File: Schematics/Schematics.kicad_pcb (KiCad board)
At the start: 2 copper layers, 60.5 x 84 mm, 14 parts, among them U1 XIAO ESP32C3, U2 TP4056-42-ESOP8

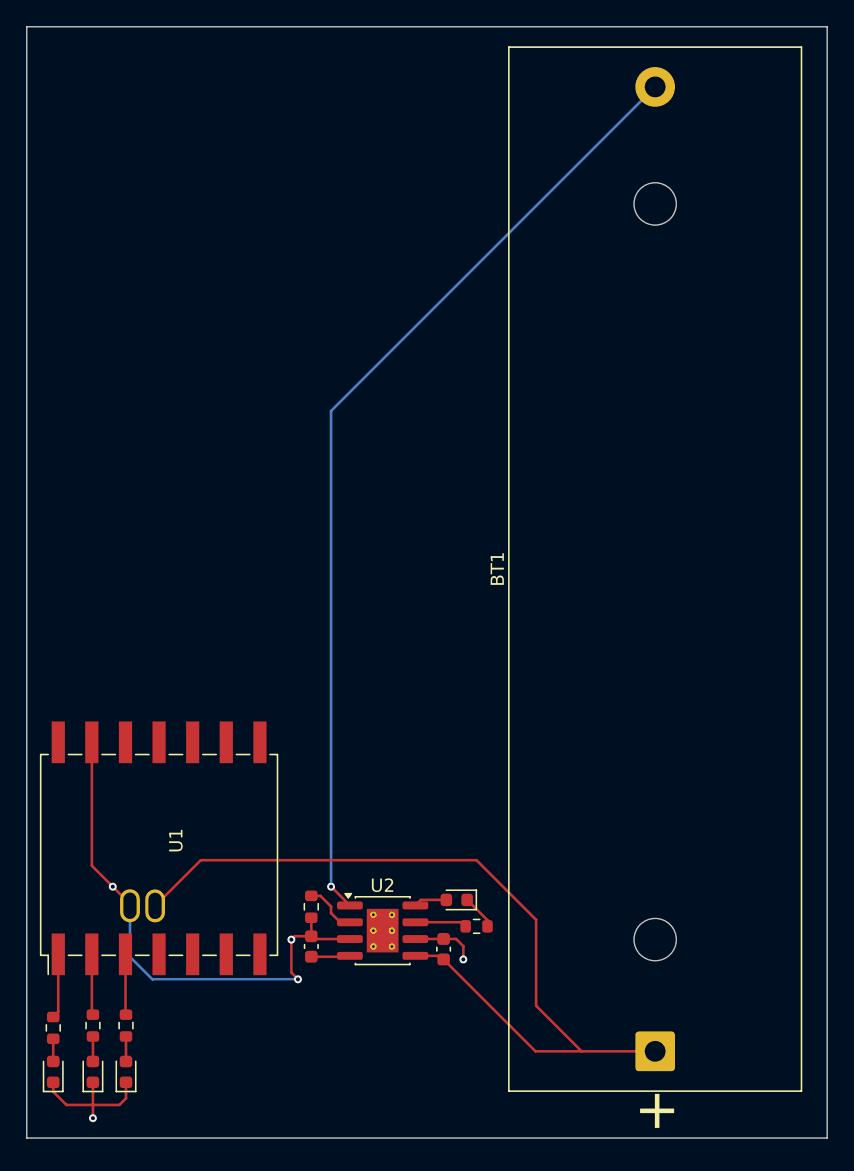
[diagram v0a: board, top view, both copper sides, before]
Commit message: redesign of the display and LEDs
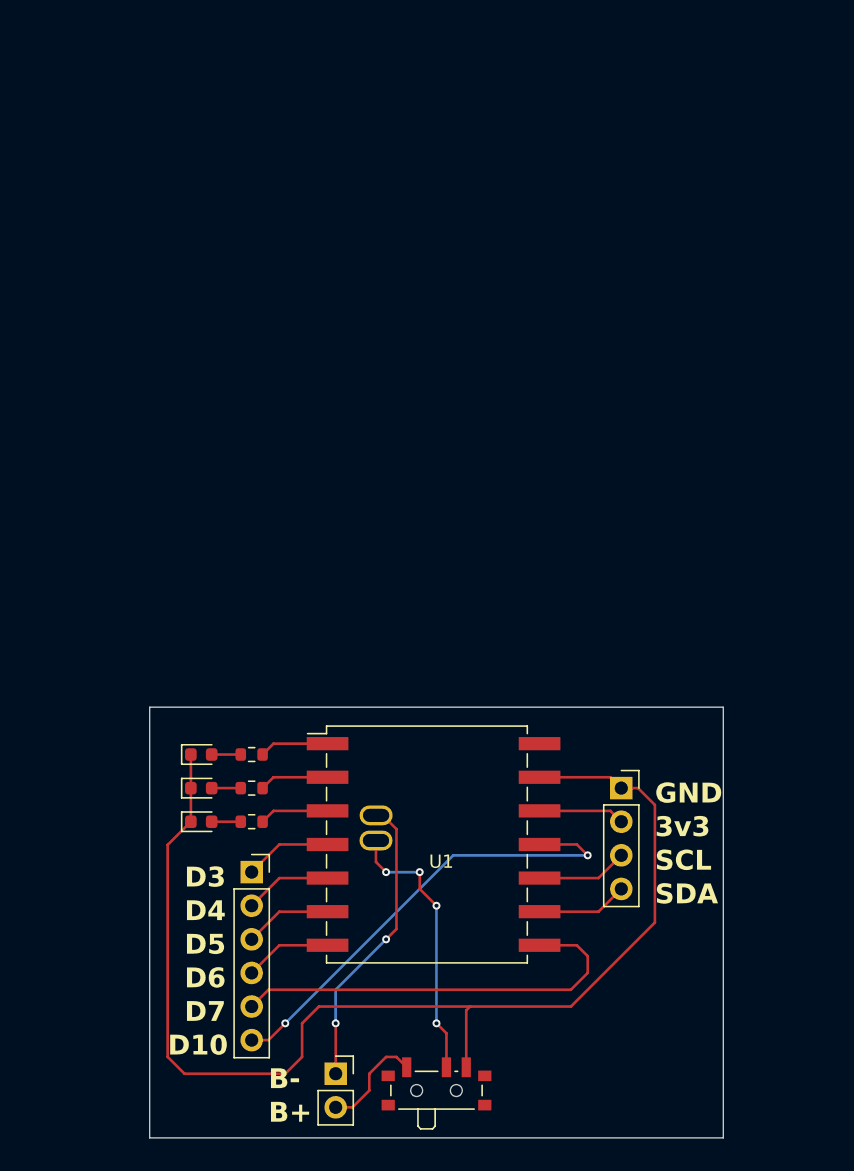
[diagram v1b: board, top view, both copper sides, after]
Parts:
- removed BT1: Battery_Cell, Battery:BatteryHolder_MPD_BH-18650-PC
- removed C1, C2: 10uF, Capacitor_SMD:C_0603_1608Metric
- removed D1: LED, LED_SMD:LED_0603_1608Metric
- removed R1: 10k, Resistor_SMD:R_0603_1608Metric
- removed R2: 1K, Resistor_SMD:R_0603_1608Metric
- removed U2: TP4056-42-ESOP8, Package_SO:SOIC-8-1EP_3.9x4.9mm_P1.27mm_EP2.41x3.3mm_ThermalVias
- added J1: Conn_01x04_Socket, Connector_PinSocket_2.54mm:PinSocket_1x04_P2.54mm_Vertical, F.Cu at (154.9, 82.5)
- added J2: Conn_01x06_Socket, Connector_PinSocket_2.54mm:PinSocket_1x06_P2.54mm_Vertical, F.Cu at (127.0, 88.9)
- added J3: Conn_01x02_Socket, Connector_PinSocket_2.54mm:PinSocket_1x02_P2.54mm_Vertical, F.Cu at (133.3, 104.1)
- added SW1: SW_SPDT, Button_Switch_SMD:SW_SPDT_PCM12, F.Cu at (141.0, 105.1)
- moved D2 26.5 mm to (123.2, 80.0), turned to 0 degrees
- moved R3 25.5 mm to (127.0, 80.0), turned to 0 degrees
- moved D3 23.0 mm to (123.2, 82.5), turned to 0 degrees
- moved R4 21.6 mm to (127.0, 82.5), turned to 0 degrees
- moved D4 19.7 mm to (123.2, 85.1), turned to 0 degrees
- moved U1 19.6 mm to (141.3, 88.6), turned to 0 degrees
- moved R5 18.1 mm to (127.0, 85.1), turned to 0 degrees
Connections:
- U1 pad 10: unconnected-(U1-D9-Pad10) -> Net-(J1-Pin_3)
- U1 pad 11: unconnected-(U1-D10-Pad11) -> Net-(J2-Pin_6)
- U1 pad 12: unconnected-(U1-VCC_3V3-Pad12) -> Net-(J1-Pin_2)
- U1 pad 4: unconnected-(U1-D3-Pad4) -> Net-(J2-Pin_1)
- U1 pad 5: unconnected-(U1-D4-Pad5) -> Net-(J2-Pin_2)
- U1 pad 6: unconnected-(U1-D5-Pad6) -> Net-(J2-Pin_3)
- U1 pad 7: unconnected-(U1-D6-Pad7) -> Net-(J2-Pin_4)
- U1 pad 8: unconnected-(U1-D7-Pad8) -> Net-(J2-Pin_5)
- U1 pad 9: unconnected-(U1-D8-Pad9) -> Net-(J1-Pin_4)
- U1 pad B-: GND -> Net-(J3-Pin_1)
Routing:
- net Net-(SW1-B): track 64.6 -> 20.8 mm, vias 0 -> 4
- net GND: track 128.5 -> 90.4 mm, vias 6 -> 0
- net Net-(J2-Pin_6): track 0.00 -> 35.2 mm, vias 0 -> 2
- net Net-(J2-Pin_5): track 0.00 -> 31.7 mm
- net Net-(J3-Pin_1): track 0.00 -> 22.4 mm, vias 0 -> 2
- net Net-(J3-Pin_2): track 0.00 -> 8.02 mm
- net Net-(J1-Pin_4): track 0.00 -> 6.89 mm
- net Net-(J1-Pin_3): track 0.00 -> 6.89 mm
- net Net-(J2-Pin_3): track 0.00 -> 6.60 mm
- net Net-(J2-Pin_2): track 0.00 -> 6.60 mm
- net Net-(J2-Pin_1): track 0.00 -> 6.60 mm
- net Net-(J2-Pin_4): track 0.00 -> 6.60 mm
- net Net-(J1-Pin_2): track 0.00 -> 6.52 mm
- net VCC 5V: track 5.46 -> 0.00 mm
- net Net-(U2-PROG): track 4.04 -> 0.00 mm
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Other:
- board size 60.5 x 84 mm -> 43.4 x 32.6 mm
- board text added: "3v3"
- board text added: "B+"
- board text added: "B-"
- board text added: "D10"
- board text added: "D3"
- board text added: "D4"
- board text added: "D5"
- board text added: "D6"
- board text added: "D7"
- board text added: "GND"
- board text added: "SCL"
- board text added: "SDA"
